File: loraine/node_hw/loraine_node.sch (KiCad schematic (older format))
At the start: 41 parts, among them CON1 BARREL_JACK, IC1 ATTINY2313A-S, P1 MOLEX, P2 MOLEX, P3 SOLDER_PAD, P4 ICSP, P5 OUTPUTS, P6 BUS, P7 BUS_THRU, Q1 BD679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

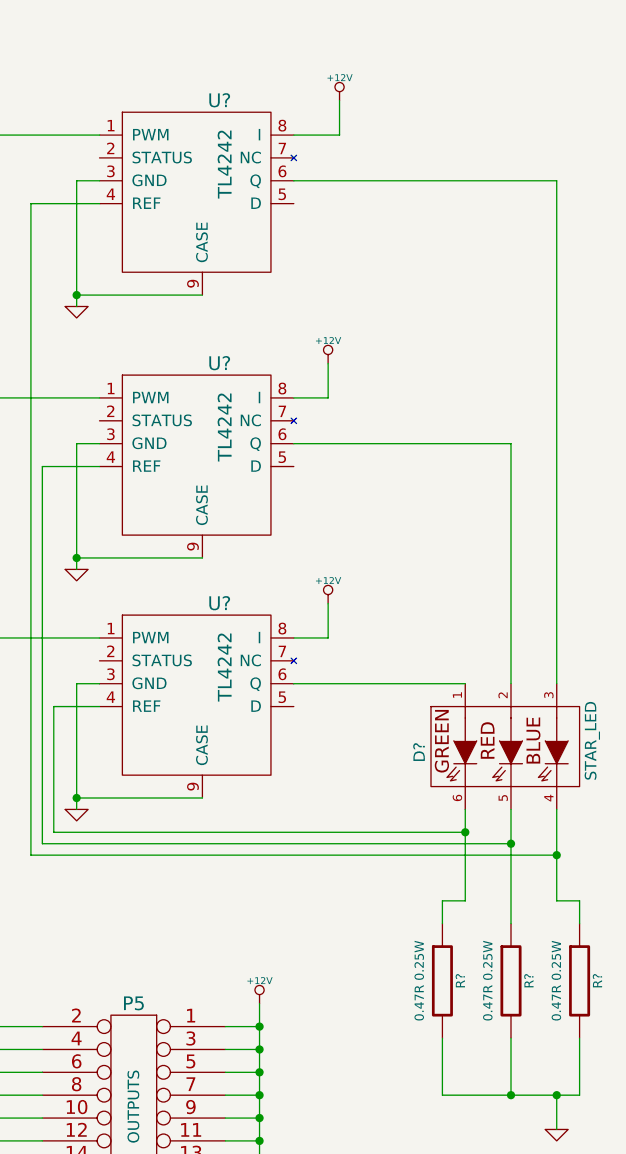
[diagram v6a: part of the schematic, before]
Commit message: Annotated schematic, annotated netlist
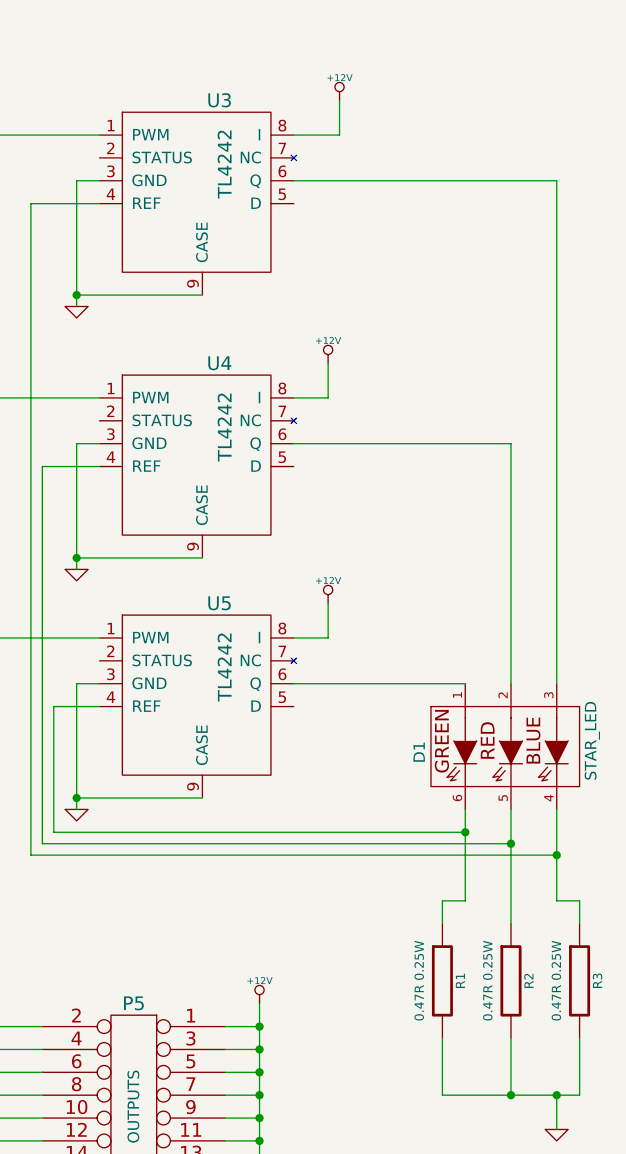
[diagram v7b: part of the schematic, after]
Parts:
- gave numbers to parts that had none: 7
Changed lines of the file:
@@
 LIBS:contrib
 LIBS:valves
-LIBS:sn65176bd
-LIBS:bd679
-LIBS:tl4242
-LIBS:star_led
 LIBS:loraine_node-cache
 EELAYER 24 0
@@
 $EndComp
 $Comp
-L VCC #PWR014
+L VCC #PWR013
 U 1 1 5339091E
 P 3200 6800
-F 0 "#PWR014" H 3200 6900 30  0001 C CNN
+F 0 "#PWR013" H 3200 6900 30  0001 C CNN
 F 1 "VCC" H 3200 6900 30  0000 C CNN
 F 2 "" H 3200 6800 60  0000 C CNN
@@
 $EndComp
 $Comp
-L +12V #PWR015
+L +12V #PWR014
 U 1 1 53390BA6
 P 9300 5250
-F 0 "#PWR015" H 9300 5200 20  0001 C CNN
+F 0 "#PWR014" H 9300 5200 20  0001 C CNN
 F 1 "+12V" H 9300 5350 30  0000 C CNN
 F 2 "" H 9300 5250 60  0000 C CNN
@@
 $EndComp
 $Comp
-L GND #PWR016
+L GND #PWR015
 U 1 1 5339D1EB
 P 2700 6900
-F 0 "#PWR016" H 2700 6900 30  0001 C CNN
+F 0 "#PWR015" H 2700 6900 30  0001 C CNN
 F 1 "GND" H 2700 6830 30  0001 C CNN
 F 2 "" H 2700 6900 60  0000 C CNN
@@
 	7950 5350 8350 5350
 $Comp
-L TL4242 U?
+L TL4242 U3
 U 1 1 5339EB06
 P 8550 2200
-F 0 "U?" H 9125 3100 60  0000 C CNN
+F 0 "U3" H 9125 3100 60  0000 C CNN
 F 1 "TL4242" V 9150 2825 60  0000 C CNN
 F 2 "" H 9175 2700 60  0000 C CNN
@@
 $EndComp
 $Comp
-L TL4242 U?
+L TL4242 U4
 U 1 1 5339EB1A
 P 8550 3350
-F 0 "U?" H 9125 4250 60  0000 C CNN
+F 0 "U4" H 9125 4250 60  0000 C CNN
 F 1 "TL4242" V 9150 3975 60  0000 C CNN
 F 2 "" H 9175 3850 60  0000 C CNN
@@
 $EndComp
 $Comp
-L TL4242 U?
+L TL4242 U5
 U 1 1 5339EB2E
 P 8550 4400
-F 0 "U?" H 9125 5300 60  0000 C CNN
+F 0 "U5" H 9125 5300 60  0000 C CNN
 F 1 "TL4242" V 9150 5025 60  0000 C CNN
 F 2 "" H 9175 4900 60  0000 C CNN
@@
 	7850 2600 7850 5450
 $Comp
-L GND #PWR?
+L GND #PWR016
 U 1 1 5339EE64
 P 10600 5800
-F 0 "#PWR?" H 10600 5800 30  0001 C CNN
+F 0 "#PWR016" H 10600 5800 30  0001 C CNN
 F 1 "GND" H 10600 5730 30  0001 C CNN
 F 2 "" H 10600 5800 60  0000 C CNN
@@
 	9450 2800 10400 2800
 $Comp
-L +12V #PWR?
+L +12V #PWR017
 U 1 1 5339ED35
 P 9650 1300
-F 0 "#PWR?" H 9650 1250 20  0001 C CNN
+F 0 "#PWR017" H 9650 1250 20  0001 C CNN
 F 1 "+12V" H 9650 1400 30  0000 C CNN
 F 2 "" H 9650 1300 60  0000 C CNN
@@
 $EndComp
 $Comp
-L GND #PWR?
+L GND #PWR018
 U 1 1 5339F02D
 P 8500 2200
-F 0 "#PWR?" H 8500 2200 30  0001 C CNN
+F 0 "#PWR018" H 8500 2200 30  0001 C CNN
 F 1 "GND" H 8500 2130 30  0001 C CNN
 F 2 "" H 8500 2200 60  0000 C CNN
@@
 Connection ~ 8500 2150
 $Comp
-L GND #PWR?
+L GND #PWR019
 U 1 1 5339F1BC
 P 8500 3350
-F 0 "#PWR?" H 8500 3350 30  0001 C CNN
+F 0 "#PWR019" H 8500 3350 30  0001 C CNN
 F 1 "GND" H 8500 3280 30  0001 C CNN
 F 2 "" H 8500 3350 60  0000 C CNN
@@
 Connection ~ 8500 3300
 $Comp
-L GND #PWR?
+L GND #PWR020
 U 1 1 5339F354
 P 8500 4400
-F 0 "#PWR?" H 8500 4400 30  0001 C CNN
+F 0 "#PWR020" H 8500 4400 30  0001 C CNN
 F 1 "GND" H 8500 4330 30  0001 C CNN
 F 2 "" H 8500 4400 60  0000 C CNN
@@
 	6000 1450 8600 1450
 $Comp
-L R R?
+L R R1
 U 1 1 5339FA1A
 P 10100 5150
-F 0 "R?" V 10180 5150 40  0000 C CNN
+F 0 "R1" V 10180 5150 40  0000 C CNN
 F 1 "0.47R 0.25W" V 10000 5150 40  0000 C CNN
 F 2 "" V 10030 5150 30  0000 C CNN
@@
 $EndComp
 $Comp
-L R R?
+L R R2
 U 1 1 5339FA2E
 P 10400 5150
-F 0 "R?" V 10480 5150 40  0000 C CNN
+F 0 "R2" V 10480 5150 40  0000 C CNN
 F 1 "0.47R 0.25W" V 10300 5150 40  0000 C CNN
 F 2 "" V 10330 5150 30  0000 C CNN
@@
 $EndComp
 $Comp
-L R R?
+L R R3
 U 1 1 5339FA42
 P 10700 5150
-F 0 "R?" V 10780 5150 40  0000 C CNN
+F 0 "R3" V 10780 5150 40  0000 C CNN
 F 1 "0.47R 0.25W" V 10600 5150 40  0000 C CNN
 F 2 "" V 10630 5150 30  0000 C CNN
@@
 	9650 1450 9450 1450
 $Comp
-L +12V #PWR?
+L +12V #PWR021
 U 1 1 533A12D0
 P 9600 2450
-F 0 "#PWR?" H 9600 2400 20  0001 C CNN
+F 0 "#PWR021" H 9600 2400 20  0001 C CNN
 F 1 "+12V" H 9600 2550 30  0000 C CNN
 F 2 "" H 9600 2450 60  0000 C CNN
@@
 	9600 2600 9600 2450
 $Comp
-L +12V #PWR?
+L +12V #PWR022
 U 1 1 533A13CA
 P 9600 3500
-F 0 "#PWR?" H 9600 3450 20  0001 C CNN
+F 0 "#PWR022" H 9600 3450 20  0001 C CNN
 F 1 "+12V" H 9600 3600 30  0000 C CNN
 F 2 "" H 9600 3500 60  0000 C CNN
@@
 	10400 5400 10400 5650
 $Comp
-L STAR_LED D?
+L STAR_LED D1
 U 1 1 53619F29
 P 10400 4150
-F 0 "D?" V 10000 4150 50  0000 C CNN
+F 0 "D1" V 10000 4150 50  0000 C CNN
 F 1 "STAR_LED" V 10750 4200 50  0000 C CNN
 F 2 "" V 10200 4050 60  0000 C CNN

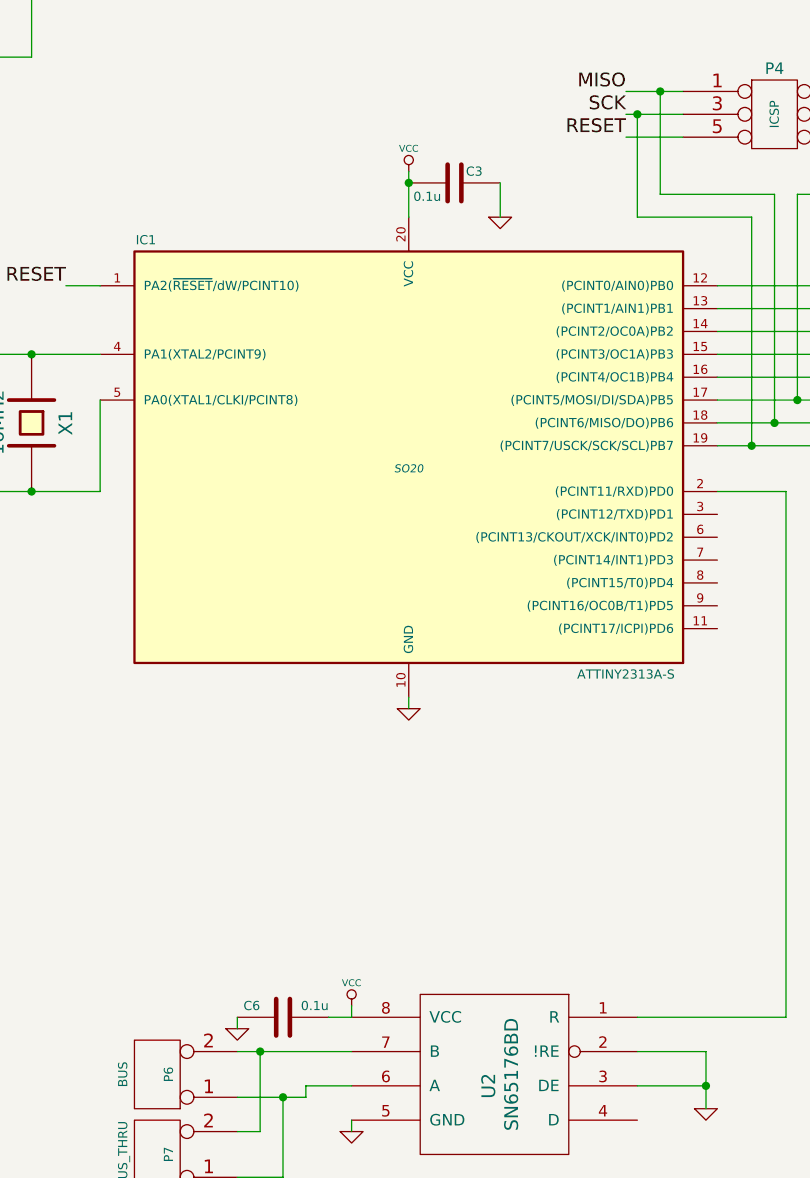
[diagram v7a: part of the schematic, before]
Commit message: Added remaining footprints to netlist/pcb
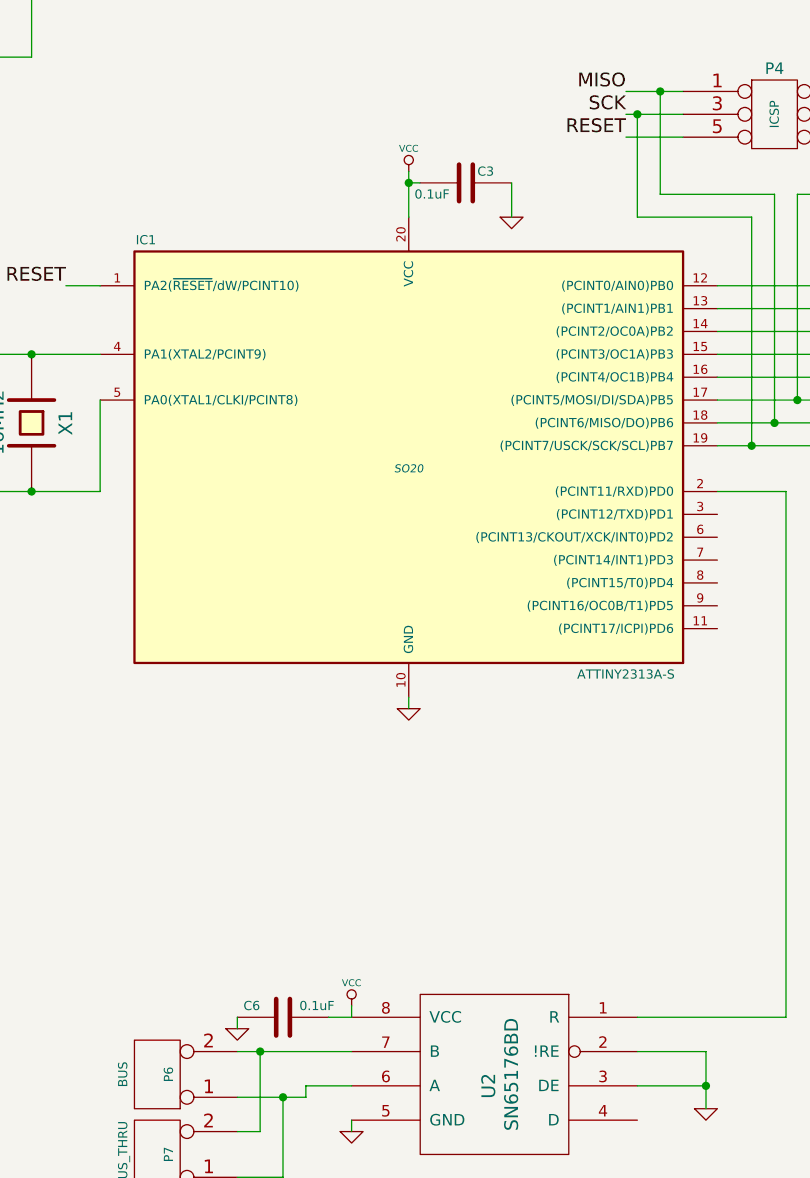
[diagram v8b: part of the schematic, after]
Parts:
- C3, C6: value 0.1u -> 0.1uF
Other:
- moved on the sheet: C3
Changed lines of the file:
@@
 P 2900 6850
 F 0 "C6" V 2950 6950 40  0000 L CNN
-F 1 "0.1u" V 2950 6650 40  0000 L CNN
+F 1 "0.1uF" V 2950 6625 40  0000 L CNN
 F 2 "" H 2938 6700 30  0000 C CNN
 F 3 "" H 2900 6850 60  0000 C CNN
@@
 L C C3
 U 1 1 5338AB56
-P 3650 3200
-F 0 "C3" V 3600 3250 40  0000 L CNN
-F 1 "0.1u" V 3710 3020 40  0000 L CNN
-F 2 "" H 3688 3050 30  0000 C CNN
-F 3 "" H 3650 3200 60  0000 C CNN
-	1    3650 3200
+P 3700 3200
+F 0 "C3" V 3650 3250 40  0000 L CNN
+F 1 "0.1uF" V 3750 2975 40  0000 L CNN
+F 2 "" H 3738 3050 30  0000 C CNN
+F 3 "" H 3700 3200 60  0000 C CNN
+	1    3700 3200
 	0    1    1    0
 $EndComp
@@
 L GND #PWR05
 U 1 1 5338AC70
-P 3850 3350
-F 0 "#PWR05" H 3850 3350 30  0001 C CNN
-F 1 "GND" H 3850 3280 30  0001 C CNN
-F 2 "" H 3850 3350 60  0000 C CNN
-F 3 "" H 3850 3350 60  0000 C CNN
-	1    3850 3350
+P 3900 3350
+F 0 "#PWR05" H 3900 3350 30  0001 C CNN
+F 1 "GND" H 3900 3280 30  0001 C CNN
+F 2 "" H 3900 3350 60  0000 C CNN
+F 3 "" H 3900 3350 60  0000 C CNN
+	1    3900 3350
 	1    0    0    -1
 $EndComp
@@
 Connection ~ 3450 3200
 Wire Wire Line
-	3850 3200 3850 3350
+	3900 3200 3900 3350
 Wire Wire Line
 	1600 1150 1600 2450
@@
 Wire Wire Line
 	10700 4800 10600 4800
+Wire Wire Line
+	3500 3200 3450 3200
 $EndSCHEMATC
